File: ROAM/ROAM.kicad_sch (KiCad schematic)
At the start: 11 parts, among them J1 CommanderX16Expansion Alt, U1 SST39SF040 (ROM), U2 74HCT00, U3 74HCT138, U4 AS6C4008 (RAM)

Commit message: Add NVRAM, add edge connector sym/fp to proj
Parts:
- removed J1: CommanderX16Expansion Alt, CommanderX16Expansion:CommanderX16Cartridge, symbol CommanderX16Expansion:CommanderX16Expansion Alt
- added C5: 100nF, Capacitor_THT:C_Axial_L3.8mm_D2.6mm_P7.50mm_Horizontal, symbol Device:C_Small
- added J1: CommanderX16Expansion Alt, X16Expansion:CommanderX16Cartridge, symbol X16_Expansion:CommanderX16Expansion Alt
- added R2, R3: 100K, Resistor_THT:R_Axial_DIN0204_L3.6mm_D1.6mm_P5.08mm_Horizontal, symbol Device:R_Small
- added SW1: SW_DIP_x04, Button_Switch_THT:SW_DIP_SPSTx04_Slide_9.78x12.34mm_W7.62mm_P2.54mm, symbol Switch:SW_DIP_x04
- added U5: FM24C64B, Package_SO:SOIC-8_3.9x4.9mm_P1.27mm, symbol Memory_NVRAM:FM24C64B
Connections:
- net +5V: now also C5.2, J1.4 (+5V), J1.57 (+5V), R2.1, R3.2, U5.8 (VDD)
- net A0: now also J1.31 (A0)
- net A1: now also J1.33 (A1)
- net A10: now also J1.51 (A10)
- net A11: now also J1.53 (A11)
- net A12: now also J1.52 (A12)
- net A13: now also J1.50 (A13)
- net A14: now also J1.48 (A14)
- net A15: now also J1.46 (A15)
- net A2: now also J1.35 (A2)
- net A3: now also J1.37 (A3)
- net A4: now also J1.39 (A4)
- net A5: now also J1.41 (A5)
- net A6: now also J1.43 (A6)
- net A7: now also J1.45 (A7)
- net A8: now also J1.47 (A8)
- net A9: now also J1.49 (A9)
- net D0: now also J1.30 (D0)
- net D1: now also J1.32 (D1)
- net D2: now also J1.34 (D2)
- net D3: now also J1.36 (D3)
- net D4: now also J1.38 (D4)
- net D5: now also J1.40 (D5)
- net D6: now also J1.42 (D6)
- net D7: now also J1.44 (D7)
- net GND: now also C5.1, J1.3 (GND), J1.55 (GND), J1.58 (GND), J1.6 (GND), SW1.4, U5.4 (VSS)
- net PHI2: now also J1.24 (PHI2)
- net ROMB0: now also J1.10 (ROMB0)
- net ROMB1: now also J1.12 (ROMB1)
- net ROMB2: now also J1.16 (ROMB2)
- net ROMB3: now also J1.20 (ROMB3)
- net ROMB4: now also J1.22 (ROMB4)
- net ROMB5: now also J1.18 (ROMB5)
- net ROMB6: now also J1.14 (ROMB6)
- net ROMB7: now also J1.8 (ROMB7)
- net RWB: now also J1.26 (RWB)
- new net: R2.2, SW1.1, SW1.2, SW1.3
- new net: J1.1 (-12V), J1.60 (-12V)
- new net: J1.2 (+12V), J1.59 (+12V)
- new net FA0: SW1.8, U5.1 (A0)
- new net FA1: SW1.7, U5.2 (A1)
- new net FA2: SW1.6, U5.3 (A2)
- new net SCL: J1.56 (SCL), U5.6 (SCL)
- new net SDA: J1.54 (SDA), U5.5 (SDA)
- new net WP: R3.1, SW1.5, U5.7 (WP)
- no-connect marks 24 -> 22

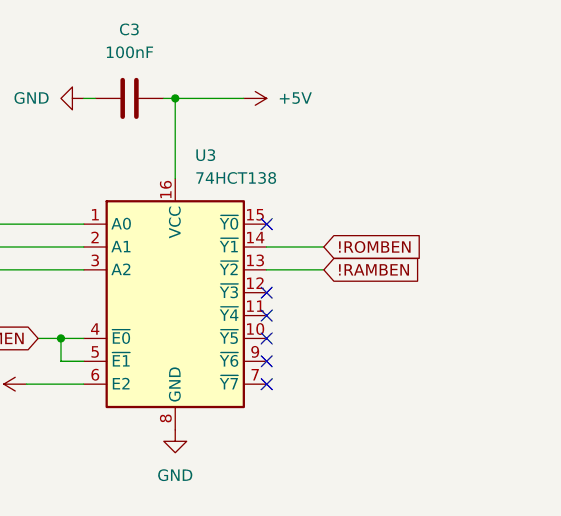
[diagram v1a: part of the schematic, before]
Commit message: Add jumpers to swap RAM/ROM
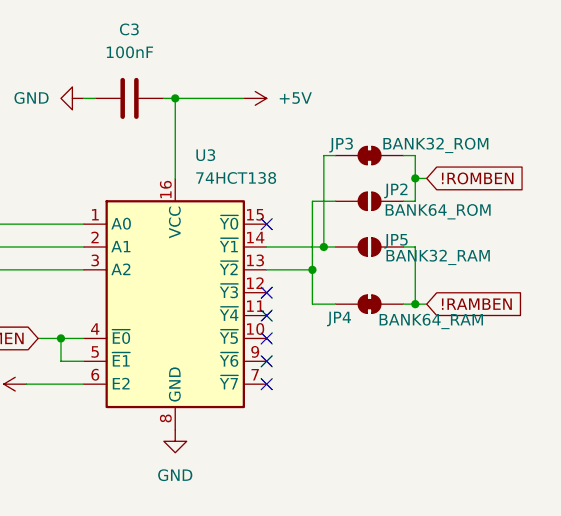
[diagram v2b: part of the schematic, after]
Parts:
- added JP2: BANK64_ROM, Jumper:SolderJumper-2_P1.3mm_Open_TrianglePad1.0x1.5mm, symbol Jumper:SolderJumper_2_Open
- added JP3: BANK32_ROM, Jumper:SolderJumper-2_P1.3mm_Bridged_Pad1.0x1.5mm, symbol Jumper:SolderJumper_2_Bridged
- added JP4: BANK64_RAM, Jumper:SolderJumper-2_P1.3mm_Bridged_Pad1.0x1.5mm, symbol Jumper:SolderJumper_2_Bridged
- added JP5: BANK32_RAM, Jumper:SolderJumper-2_P1.3mm_Open_TrianglePad1.0x1.5mm, symbol Jumper:SolderJumper_2_Open
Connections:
- net !RAMBEN: now also JP4.2 (B), JP5.1 (A); no longer U3.13 (~{Y2})
- net !ROMBEN: now also JP2.1 (A), JP3.2 (B); no longer U3.14 (~{Y1})
- new net: JP3.1 (A), JP5.2 (B), U3.14 (~{Y1})
- new net: JP2.2 (B), JP4.1 (A), U3.13 (~{Y2})

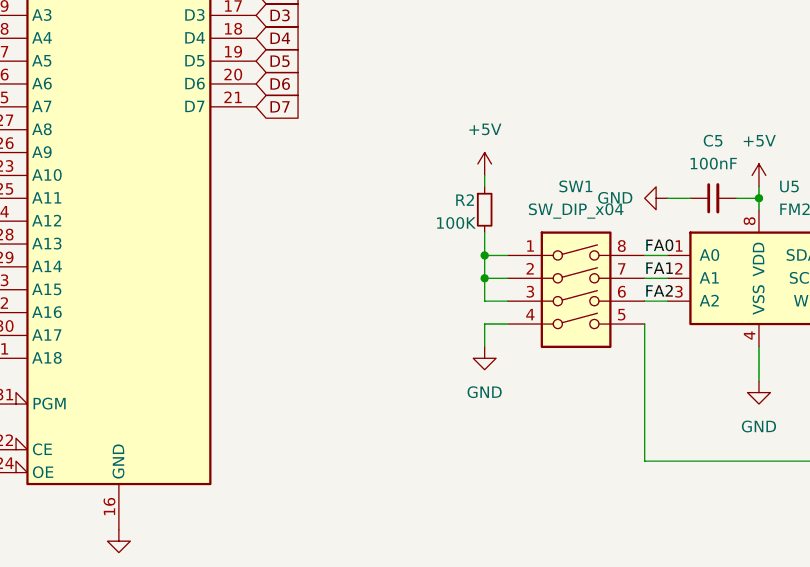
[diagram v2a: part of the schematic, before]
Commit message: Rounded connector edges; switched caps; NVRAM addr solder jumpers
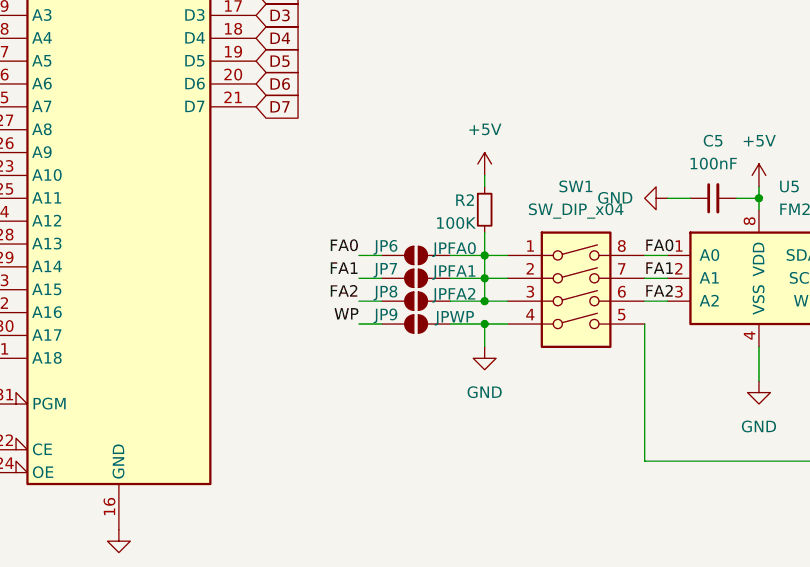
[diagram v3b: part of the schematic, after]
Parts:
- added JP6: JPFA0, Jumper:SolderJumper-2_P1.3mm_Open_TrianglePad1.0x1.5mm, symbol Jumper:SolderJumper_2_Open
- added JP7: JPFA1, Jumper:SolderJumper-2_P1.3mm_Open_TrianglePad1.0x1.5mm, symbol Jumper:SolderJumper_2_Open
- added JP8: JPFA2, Jumper:SolderJumper-2_P1.3mm_Open_TrianglePad1.0x1.5mm, symbol Jumper:SolderJumper_2_Open
- added JP9: JPWP, Jumper:SolderJumper-2_P1.3mm_Open_TrianglePad1.0x1.5mm, symbol Jumper:SolderJumper_2_Open
- C1, C2, C3, C4, C5: footprint Capacitor_THT:C_Axial_L3.8mm_D2.6mm_P7.50mm_Horizontal -> Capacitor_THT:C_Disc_D4.3mm_W1.9mm_P5.00mm
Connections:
- net FA0: now also JP6.2 (B)
- net FA1: now also JP7.2 (B)
- net FA2: now also JP8.2 (B)
- net GND: now also JP9.1 (A)
- net WP: now also JP9.2 (B)
- net at R2.2, SW1.1, SW1.2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: now also JP6.1 (A), JP7.1 (A), JP8.1 (A)
